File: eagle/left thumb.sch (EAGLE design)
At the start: 12 parts, among them J1 B7B-ZR_(LF)(SN)

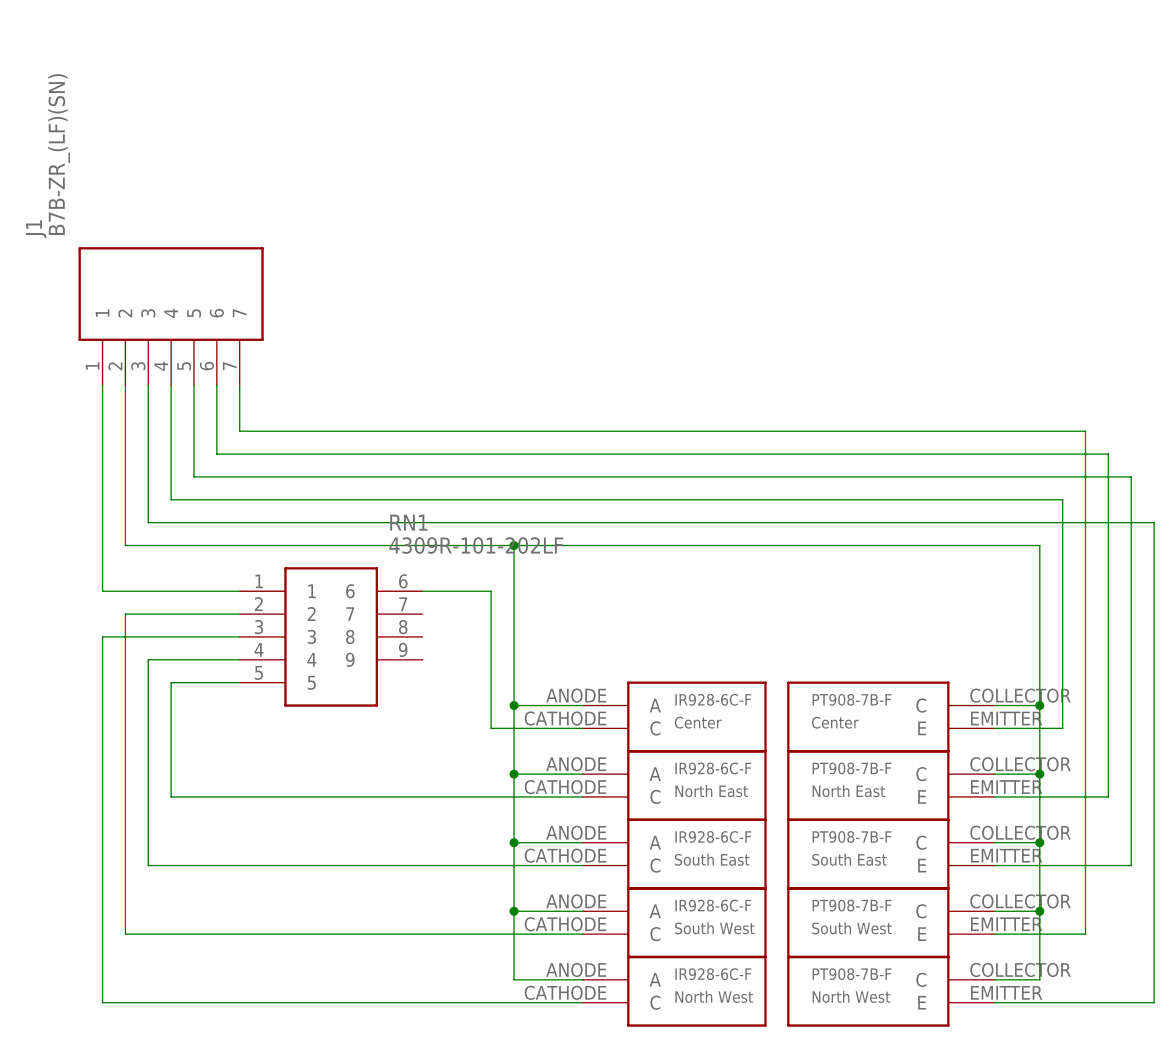
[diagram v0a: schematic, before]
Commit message: Fix drill holes and outer dimensions on cluster and left thumb cluster
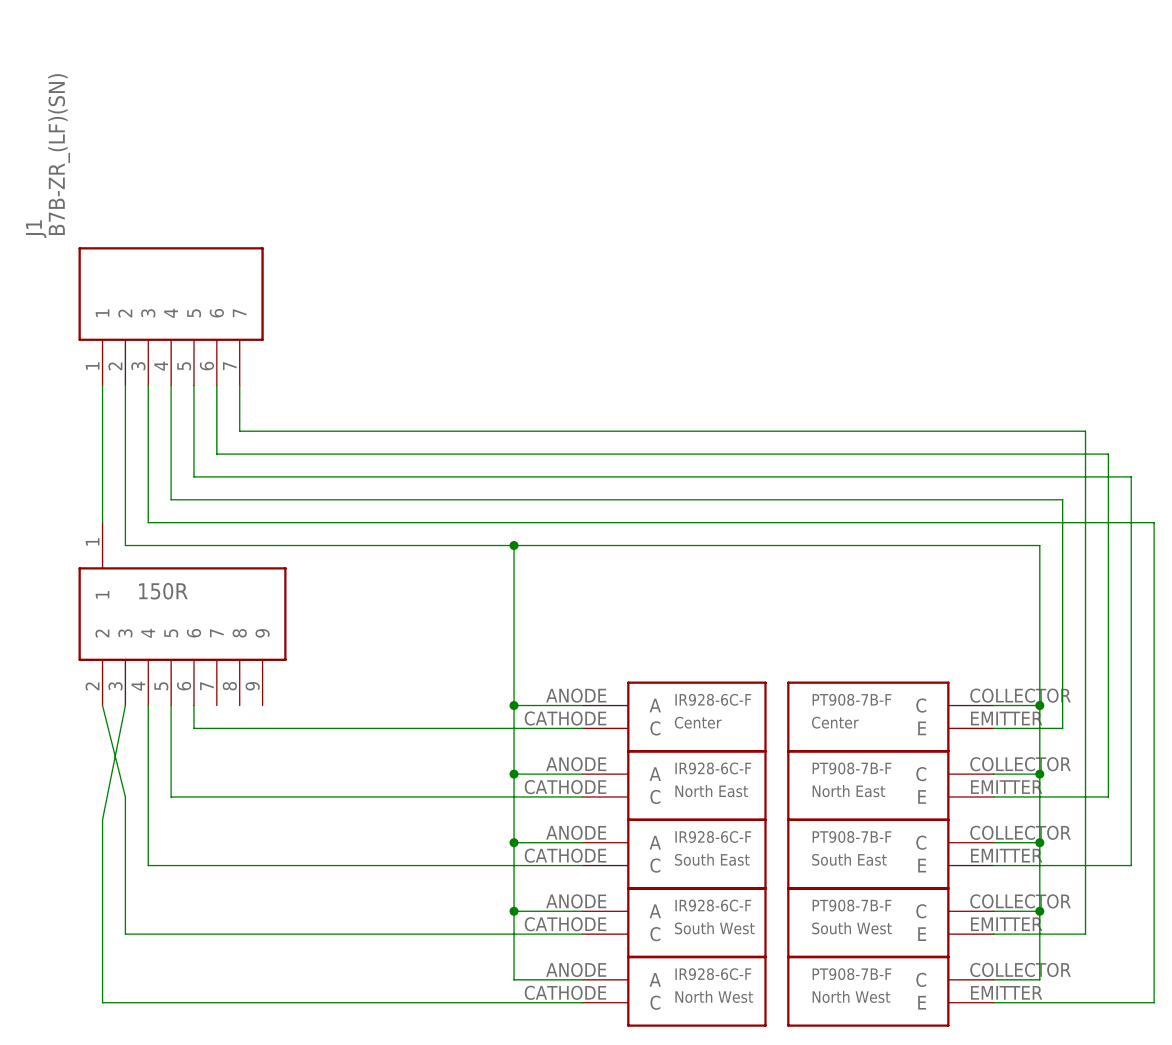
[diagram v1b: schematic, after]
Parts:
- RN1: value 4309R-101-202LF -> 150R; device 4309R-101-202LF:4309R-101-202LF -> 9 pin resistor network:9PIN-RESISTOR-NETWORK9PIN-RESISTOR-NETWORK
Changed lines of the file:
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@@
 <?xml version="1.0" encoding="utf-8"?>
 <!DOCTYPE eagle SYSTEM "eagle.dtd">
-<eagle version="9.3.2">
+<eagle version="9.4.2">
 <drawing>
 <settings>
@@
 <part name="LED5" library="IR928-6C-F" deviceset="IR928-6C-F" device="" value="North West"/>
 <part name="J1" library="SamacSys_Parts" deviceset="B7B-ZR_(LF)(SN)" device=""/>
-<part name="RN1" library="4309R-101-202LF" deviceset="4309R-101-202LF" device=""/>
+<part name="RN1" library="9 pin resistor network" deviceset="9PIN-RESISTOR-NETWORK" device="9PIN-RESISTOR-NETWORK" value="150R"/>
 </parts>
 <sheets>
@@
 <attribute name="VALUE" x="7.62" y="90.17" size="1.778" layer="96" rot="R90" align="center-left"/>
 </instance>
-<instance part="RN1" gate="G$1" x="27.94" y="50.8" smashed="yes">
-<attribute name="NAME" x="44.45" y="58.42" size="1.778" layer="95" align="center-left"/>
-<attribute name="VALUE" x="44.45" y="55.88" size="1.778" layer="96" align="center-left"/>
+<instance part="RN1" gate="G$1" x="12.7" y="58.42" smashed="yes">
+<attribute name="VALUE" x="16.51" y="50.8" size="1.778" layer="96" align="center-left"/>
 </instance>
 </instances>
@@
 <pinref part="J1" gate="G$1" pin="1"/>
 <pinref part="RN1" gate="G$1" pin="1"/>
-<wire x1="12.7" y1="73.66" x2="12.7" y2="50.8" width="0.1524" layer="91"/>
-<wire x1="12.7" y1="50.8" x2="27.94" y2="50.8" width="0.1524" layer="91"/>
+<wire x1="12.7" y1="73.66" x2="12.7" y2="58.42" width="0.1524" layer="91"/>
 </segment>
 </net>
@@
 <segment>
 <pinref part="LED5" gate="G$1" pin="C"/>
-<wire x1="12.7" y1="45.72" x2="12.7" y2="5.08" width="0.1524" layer="91"/>
+<wire x1="12.7" y1="25.4" x2="12.7" y2="5.08" width="0.1524" layer="91"/>
 <wire x1="12.7" y1="5.08" x2="66.04" y2="5.08" width="0.1524" layer="91"/>
 <pinref part="RN1" gate="G$1" pin="3"/>
-<wire x1="27.94" y1="45.72" x2="12.7" y2="45.72" width="0.1524" layer="91"/>
+<wire x1="15.24" y1="38.1" x2="12.7" y2="25.4" width="0.1524" layer="91"/>
 </segment>
 </net>
@@
 <pinref part="LED4" gate="G$1" pin="C"/>
 <wire x1="66.04" y1="12.7" x2="15.24" y2="12.7" width="0.1524" layer="91"/>
-<wire x1="15.24" y1="12.7" x2="15.24" y2="48.26" width="0.1524" layer="91"/>
+<wire x1="15.24" y1="12.7" x2="15.24" y2="27.94" width="0.1524" layer="91"/>
 <pinref part="RN1" gate="G$1" pin="2"/>
-<wire x1="15.24" y1="48.26" x2="27.94" y2="48.26" width="0.1524" layer="91"/>
+<wire x1="15.24" y1="27.94" x2="12.7" y2="38.1" width="0.1524" layer="91"/>
 </segment>
 </net>
@@
 <segment>
 <pinref part="RN1" gate="G$1" pin="4"/>
-<wire x1="27.94" y1="43.18" x2="17.78" y2="43.18" width="0.1524" layer="91"/>
-<wire x1="17.78" y1="43.18" x2="17.78" y2="20.32" width="0.1524" layer="91"/>
+<wire x1="17.78" y1="38.1" x2="17.78" y2="20.32" width="0.1524" layer="91"/>
 <pinref part="LED3" gate="G$1" pin="C"/>
 <wire x1="17.78" y1="20.32" x2="66.04" y2="20.32" width="0.1524" layer="91"/>
@@
 <wire x1="66.04" y1="27.94" x2="20.32" y2="27.94" width="0.1524" layer="91"/>
 <pinref part="RN1" gate="G$1" pin="5"/>
-<wire x1="20.32" y1="27.94" x2="20.32" y2="40.64" width="0.1524" layer="91"/>
-<wire x1="20.32" y1="40.64" x2="27.94" y2="40.64" width="0.1524" layer="91"/>
+<wire x1="20.32" y1="27.94" x2="20.32" y2="38.1" width="0.1524" layer="91"/>
 </segment>
 </net>
@@
 <segment>
 <pinref part="RN1" gate="G$1" pin="6"/>
-<wire x1="48.26" y1="50.8" x2="55.88" y2="50.8" width="0.1524" layer="91"/>
-<wire x1="55.88" y1="50.8" x2="55.88" y2="35.56" width="0.1524" layer="91"/>
+<wire x1="22.86" y1="38.1" x2="22.86" y2="35.56" width="0.1524" layer="91"/>
+<wire x1="22.86" y1="35.56" x2="66.04" y2="35.56" width="0.1524" layer="91"/>
 <pinref part="LED1" gate="G$1" pin="C"/>
-<wire x1="55.88" y1="35.56" x2="66.04" y2="35.56" width="0.1524" layer="91"/>
 </segment>
 </net>
